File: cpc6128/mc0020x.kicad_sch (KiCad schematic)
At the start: 67 parts, among them IC101 74LS145, IC102 AY-3-8912, IC106 74LS273, IC107 8255A, IC108 MC6845, IC110 74LS132, IC111 Z80CPU, IC112 74LS32, IC116 AMG40010, IC117 74HCU04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

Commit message: Update title blocks
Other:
- company: Amstrad -> Amstrad plc
- title: CPC6128 -> CPC6128 MC0020x
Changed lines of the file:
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@@
   (paper "A3")
   (title_block
-    (title "CPC6128")
-    (company "Amstrad")
+    (title "CPC6128 MC0020x")
+    (date "2022-08-20")
+    (rev "1")
+    (company "Amstrad plc")
   )
   (junction (at 41.91 266.7) (diameter 0) (color 0 0 0 0)

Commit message: Fixes from new top pcb image
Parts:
- added G1: LOGO, Amstrad-CPC:LOGO, symbol CPC_Kicad_symbols:LOGO
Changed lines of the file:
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@@
     (pin "1")
+  )
+  (symbol (lib_id "CPC_Kicad_symbols:LOGO") (at 18.415 15.875 0) (unit 1)
+    (in_bom no) (on_board yes) (fields_autoplaced)
+    (property "Reference" "G1" (id 0) (at 19.05 15.0403 0)
+      (effects (font (size 1.27 1.27)) (justify left))
+    )
+    (property "Value" "LOGO" (id 1) (at 19.05 17.5772 0)
+      (effects (font (size 1.27 1.27)) (justify left))
+    )
+    (property "Footprint" "Amstrad-CPC:LOGO" (id 2) (at 18.415 15.875 0)
+      (effects (font (size 1.27 1.27)) hide)
+    )
+    (property "Datasheet" "" (id 3) (at 18.415 15.875 0)
+      (effects (font (size 1.27 1.27)) hide)
+    )
   )
   (symbol (lib_id "Device:R") (at 309.88 24.13 0) (mirror y) (unit 1)
@@
       (reference "#PWR0234") (unit 1) (value "GND") (footprint "")
     )
+    (path "/279c8db4-c686-4218-bc30-7e4827e89930/fe5471c5-86f2-4da5-a4f4-0c6c07fe7ed4"
+      (reference "#PWR0235") (unit 1) (value "GND") (footprint "")
+    )
     (path "/c64346e4-4c52-4195-be8a-3dcd177c5723"
       (reference "#PWR0901") (unit 1) (value "+5V") (footprint "")
@@
       (reference "D304") (unit 1) (value "KDS1555") (footprint "Diode_THT:D_DO-35_SOD27_P10.16mm_Horizontal")
     )
+    (path "/e0b83f1c-443c-49a6-bec5-aaa565e5f40a"
+      (reference "G1") (unit 1) (value "LOGO") (footprint "Amstrad-CPC:LOGO")
+    )
     (path "/6c1416af-5d14-423e-8d67-23c6eea78ea0"

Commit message: Minor cleanups
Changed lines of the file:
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@@
       (effects (font (size 1.27 1.27)) (justify left))
     )
-    (pin "RD_DATA" input (at 118.11 49.53 180)
+    (pin "RD_DATA" output (at 118.11 49.53 180)
       (effects (font (size 1.27 1.27)) (justify left))
     )

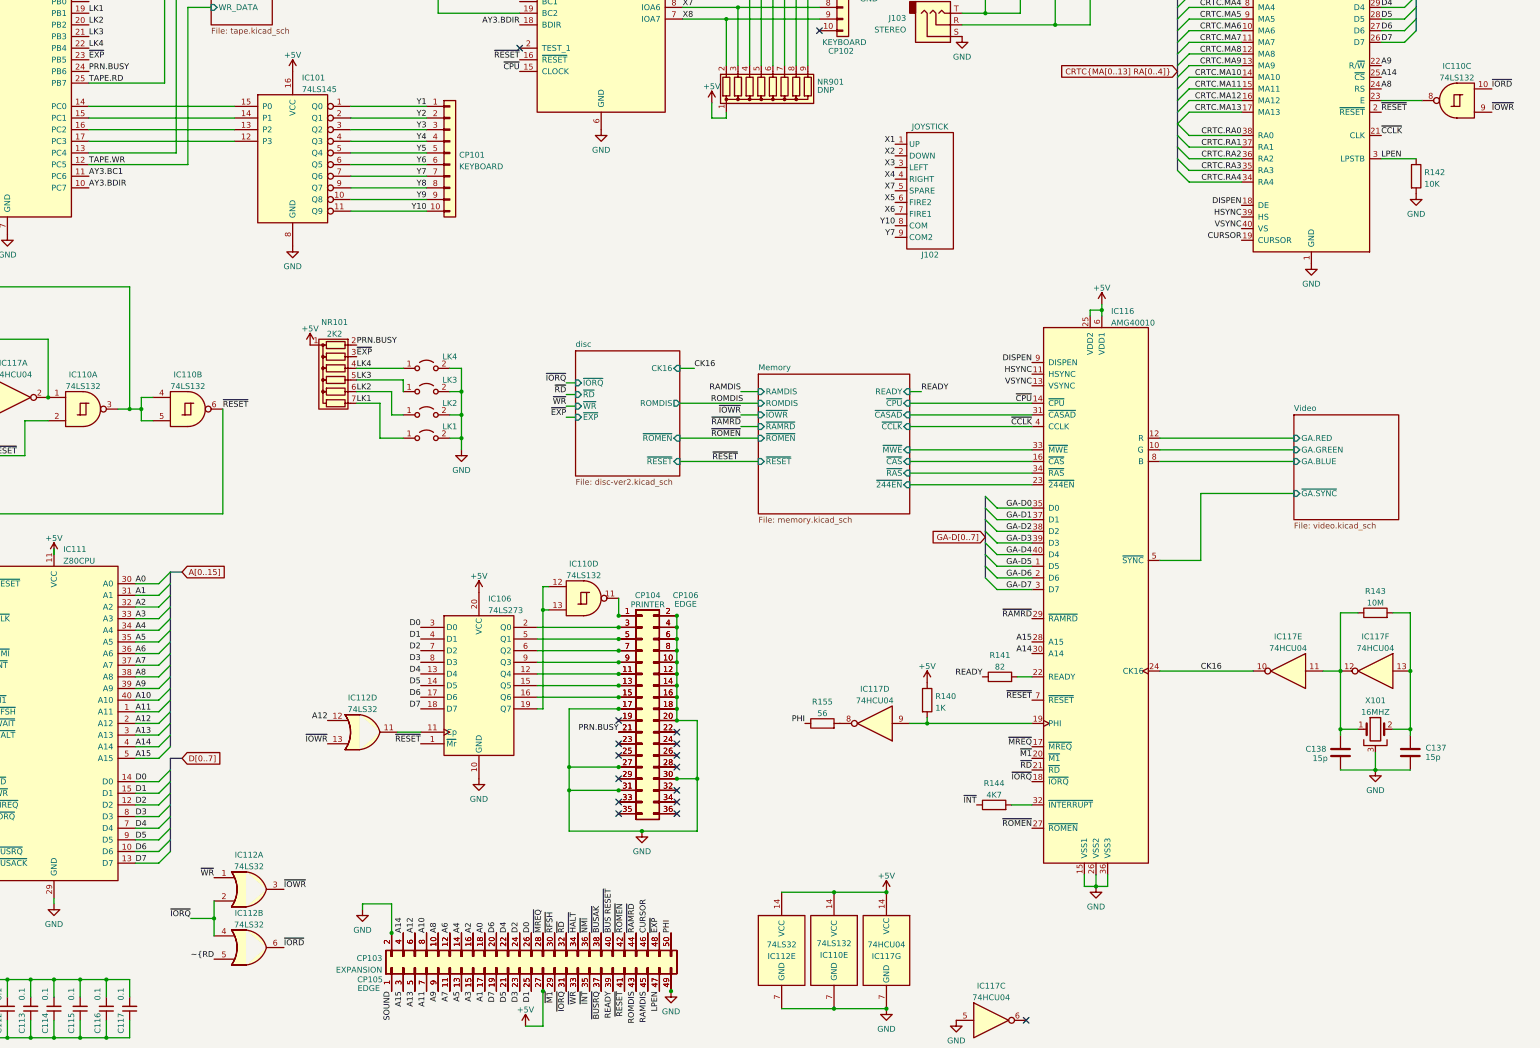
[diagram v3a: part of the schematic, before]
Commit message: Correct C136 (missing) and C314 (wrong footprint) Thanks @orzel!
Also migrated to KiCad 9.
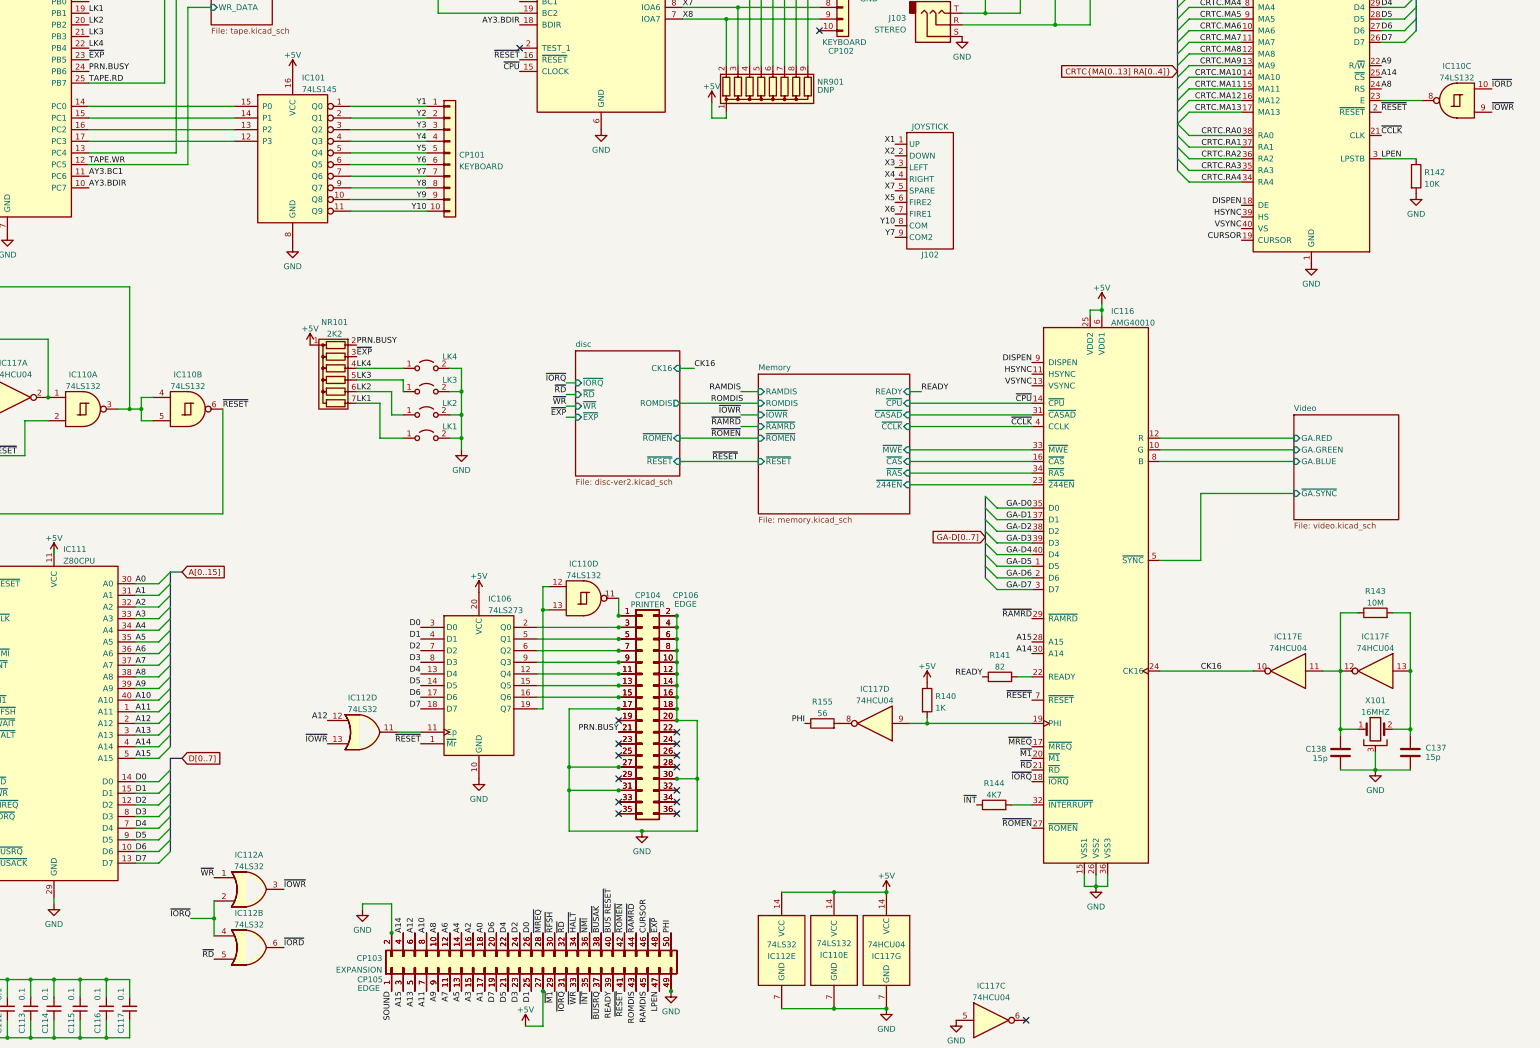
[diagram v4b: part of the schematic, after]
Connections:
- net ~{RD is gone; now on net ~{RD}: IC112.5
